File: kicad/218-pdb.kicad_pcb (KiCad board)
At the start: 2 copper layers, 80 x 55.4 mm, 73 parts, among them J1 Conn_01x03, J10 Conn_01x03, J11 Conn_01x03, J12 Conn_01x03, J13 Conn_01x03, J14 Conn_01x03, J15 Conn_01x03, J16 Conn_01x03, J17 Conn_01x03, J18 Conn_01x03, J19 Conn_01x03, J2 Conn_01x03, J20 Conn_01x03, J21 Conn_01x03, J22 Conn_01x03, J23 Conn_01x03, J24 Conn_01x03, J25 Conn_01x04_Pin, J26 Conn_01x04_Pin, J27 Conn_01x04_Pin, J28 Conn_01x04_Pin, J29 14 V molex, J3 Conn_01x03, J30 14 V molex, J31 14 V molex, J32 14 V molex, J33 external 5V, J34 battery, J35 battery, J4 Conn_01x03, J5 Conn_01x03, J6 Conn_01x03, J7 Conn_01x03, J8 Conn_01x03, J9 Conn_01x03, SW1 5V switch, U1 DC-DC buck, U2 DC-DC buck, U3 LD1117V33, U4 LD1117V33

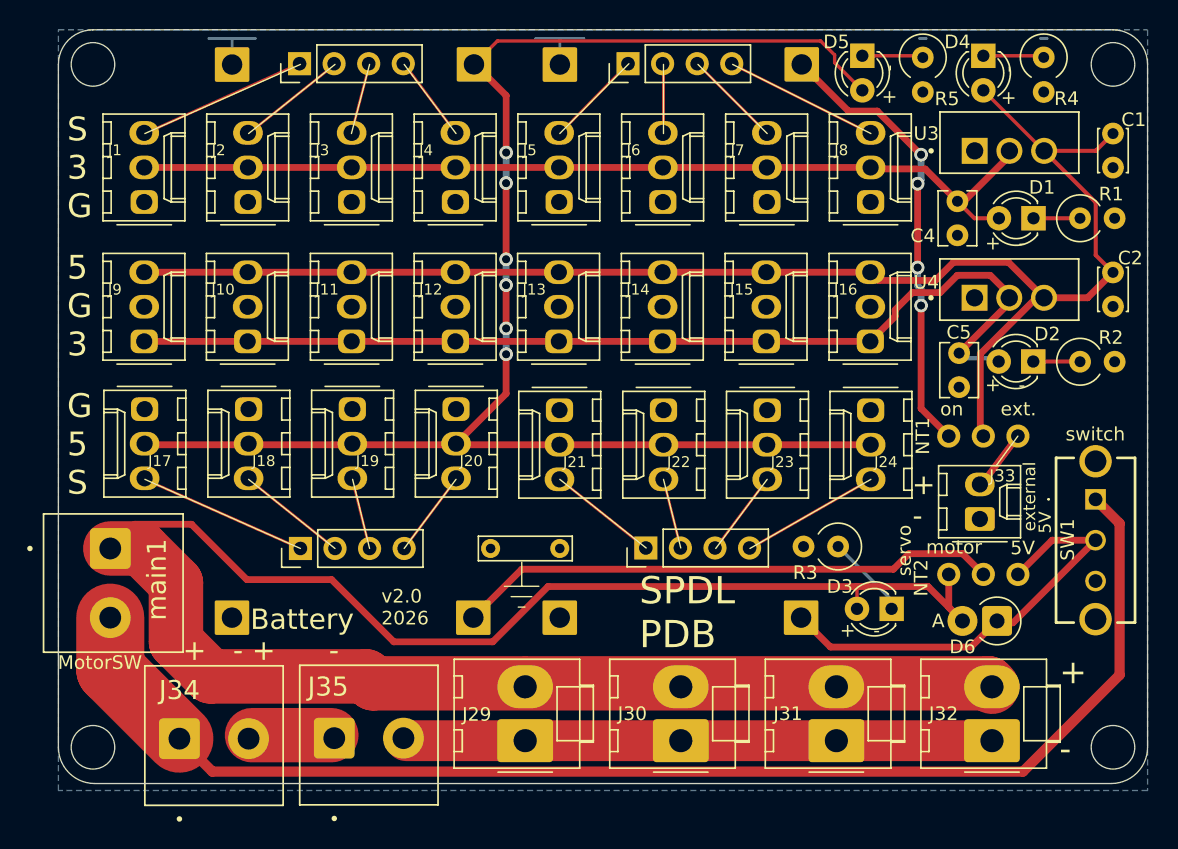
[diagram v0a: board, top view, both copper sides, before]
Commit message: improve power traces
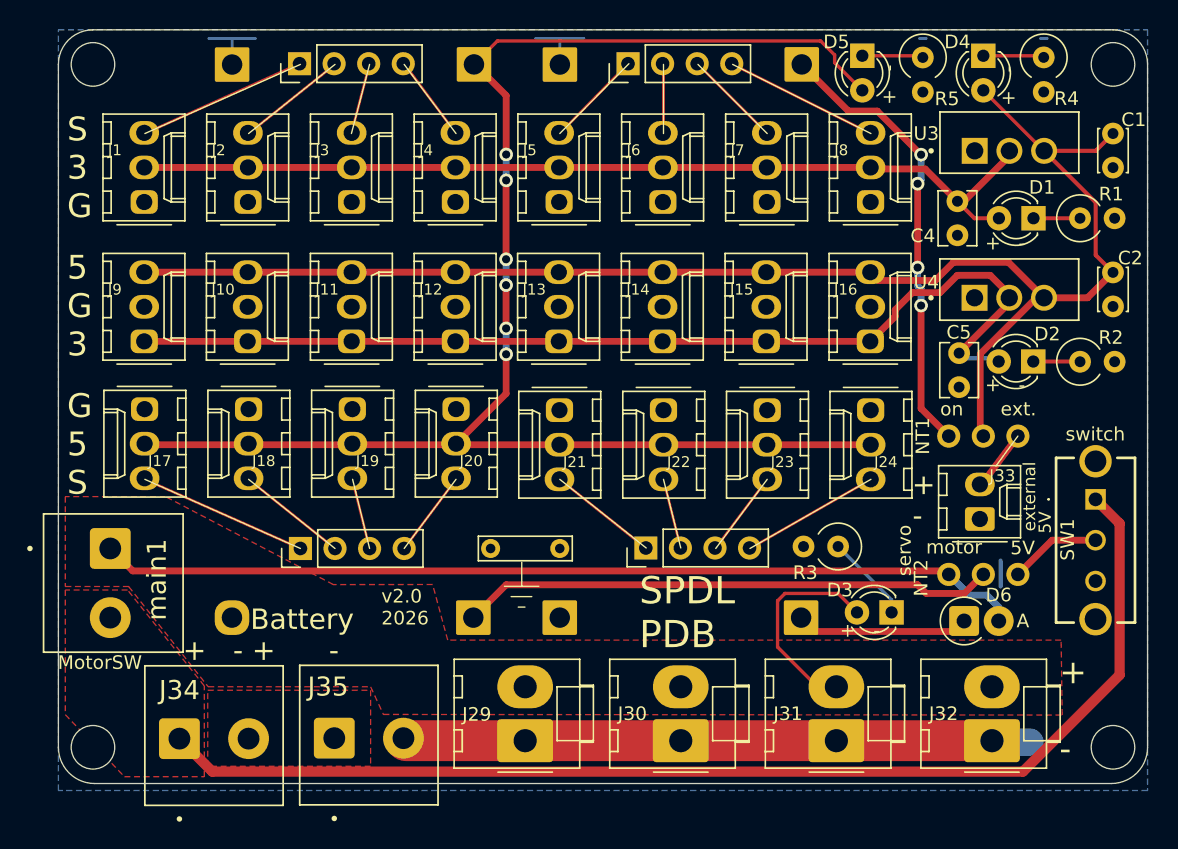
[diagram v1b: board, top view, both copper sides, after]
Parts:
- moved D6 2.42 mm to (142.7, 94.2), turned to 0 degrees
- moved D3 0.26 mm to (137.4, 93.6)
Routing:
- net 14-3: track 147.3 -> 83.6 mm
- net GND: track 54.2 -> 102.2 mm
- net 14-1: track 32.6 -> 19.5 mm
- net +BATT: track 97.6 -> 86.6 mm
- net Net-(J34-Pin_2): track 5.88 -> 0.05 mm
- net 14-2: track 40.0 -> 39.3 mm
- added copper zone on F.Cu, net +BATT
- added copper zone on F.Cu, net 14-3
- added copper zone on F.Cu, net Net-(J34-Pin_2)
